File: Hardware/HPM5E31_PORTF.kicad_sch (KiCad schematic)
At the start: 1 part, among them U1 HPM5E31IGN1

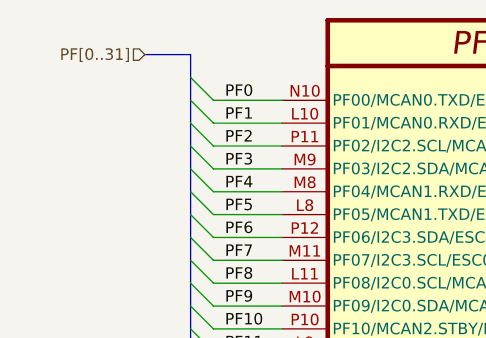
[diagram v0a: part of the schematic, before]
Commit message: 新增ESC IO引出，ESC CTR LED，EUI接口
编码器接口电源输出加保险，SPI加ESD
PY32ADC外部接口加ESD
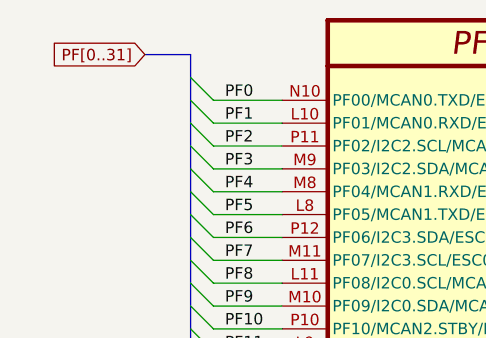
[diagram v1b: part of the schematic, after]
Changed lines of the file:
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@@
 		)
 	)
-	(hierarchical_label "PF[0..31]"
+	(global_label "PF[0..31]"
 		(shape input)
 		(at 90.17 53.34 180)
+		(fields_autoplaced yes)
 		(effects
 			(font
@@
 			(justify right)
 		)
+		(property "Intersheetrefs" "${INTERSHEET_REFS}"
+			(at 78.2947 53.34 0)
+			(effects
+				(font
+					(size 1.27 1.27)
+				)
+				(justify right)
+				(hide yes)
+			)
+		)
 	)

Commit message: 拉线
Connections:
- net PF0: now also U1.M2 (DCDC_IN); no longer U1.N10 (PF00/MCAN0.TXD/ESC0.MDC/PWM0.P0/TRGM.P00/ETH0.MDC/QEO1.A)
- net PF1: no longer U1.L10 (PF01/MCAN0.RXD/ESC0.MDIO/PWM0.P1/TRGM.P01/ETH0.MDIO/QEO1.B)
- net PF10: no longer U1.P10 (PF10/MCAN2.STBY/ESC0.P1_RXD1/PWM1.P2/TRGM.P10/ETH0.RXD1/EUI1.DI)
- net PF11: no longer U1.L9 (PF11/ESC0.P1_RXD2/PWM1.P3/TRGM.P11/ETH0.RXD2/EUI1.DO)
- net PF12: no longer U1.N11 (PF12/I2C1.SDA/ESC0.P1_RXD3/PWM1.P4/TRGM.P12/ETH0.RXD3/OWR0.DAT)
- net PF13: no longer U1.N12 (PF13/I2C1.SCL/MCAN3.STBY/ESC0.P1_RXCK/PWM1.P5/TRGM.P13/ETH0.RXCK/OWR1.DAT)
- net PF14: no longer U1.N9 (PF14/MCAN3.RXD/ESC0.P1_RXER/PWM1.P6/TRGM.P14/ETH0.RXER)
- net PF15: no longer U1.P9 (PF15/MCAN3.TXD/PWM1.P7/TRGM.P15/ETH0.TXER)
- net PF16: no longer U1.N7 (PF16/SDM0.DAT0/ADC0.IN08/ADC1.IN08/ACMP0_CH0.INN7)
- net PF17: no longer U1.P7 (PF17/SDM0.CLK0/ADC0.IN12/ADC1.IN12/ACMP0_CH1.INN7)
- net PF18: no longer U1.P8 (PF18/SDM0.DAT1/USB0.PWR/ETH0.EVTO0/ESC0.EVTO0/ADC0.IN11/ADC1.IN11/ACMP0_CH1.INP7)
- net PF19: no longer U1.M5 (PF19/SDM0.CLK1/USB0.PWR/ADC0.IN13/ADC1.IN13/ACMP0_CH0.INP7)
- net PF2: no longer U1.P11 (PF02/I2C2.SCL/MCAN0.STBY/ESC0.P1_TXCK/PWM0.P2/TRGM.P02/ETH0.TXCK/QEI0.H1/QEO1.Z/EUI0.CK)
- net PF20: no longer U1.N6 (PF20/SDM0.DAT3/USB0.OC/ETH0.EVTO1/ESC0.EVTO1/ADC0.IN03/ADC1.IN03/ACMP0_CH0.INP4/ACMP0_CH1.INP4)
- net PF21: no longer U1.L6 (PF21/SDM0.DAT2/USB0.ID/ETH0.EVTI0/ESC0.EVTI0/ADC0.IN02/ADC1.IN02/ACMP0_CH0.INN4/ACMP0_CH1.INN4)
- net PF22: no longer U1.N8 (PF22/SDM0.CLK2/USB0.ID/ETH0.EVTI1/ESC0.EVTI1/ADC0.IN14/ADC1.IN14/ACMP0_CH0.INN5/ACMP0_CH1.INN5)
- net PF23: no longer U1.L5 (PF23/SDM0.CLK3/USB0.OC/ADC0.IN15/ADC1.IN15/ACMP0_CH0.INN3/ACMP0_CH1.INN3)
- net PF24: no longer U1.M6 (PF24/SDM0.DAT0/ADC0.IN10/ADC1.IN10/ACMP0_CH0.INP5/ACMP0_CH1.INP5)
- net PF25: no longer U1.L7 (PF25/SDM0.CLK0/ADC0.IN09/ADC1.IN09/ACMP0_CH0.INP3/ACMP0_CH1.INP3)
- net PF26: no longer U1.P6 (PF26/SDM0.DAT1/ADC0.IN01/ADC1.IN01/ACMP0_CH0.INN6/ACMP0_CH1.INN6)
- net PF27: no longer U1.M7 (PF27/SDM0.CLK1/ADC0.IN00/ADC1.IN00/ACMP0_CH0.INP6/ACMP0_CH1.INP6)
- net PF28: no longer U1.P5 (PF28/SDM0.DAT3/ADC0.IN05/ADC1.IN05/ACMP0_CH0.INN2/ACMP0_CH1.INN2)
- net PF29: no longer U1.M4 (PF29/SDM0.DAT2/ADC0.IN04/ADC1.IN04/ACMP0_CH0.INP2/ACMP0_CH1.INP2)
- net PF3: now also U1.N2 (DCDC_LP); no longer U1.M9 (PF03/I2C2.SDA/MCAN1.STBY/ESC0.P1_TXD0/PWM0.P3/TRGM.P03/ETH0.TXD0/QEI0.F/EUI0.SH)
- net PF30: no longer U1.L4 (PF30/SDM0.CLK2/ADC0.IN06/ADC1.IN06/ACMP0_CH0.INN1/ACMP0_CH1.INN1)
- net PF31: no longer U1.N5 (PF31/SDM0.CLK3/ADC0.IN07/ADC1.IN07/ACMP0_CH0.INP1/ACMP0_CH1.INP1)
- net PF4: now also U1.P3 (DCDC_LP); no longer U1.M8 (PF04/MCAN1.RXD/ESC0.P1_TXD1/PWM0.P4/TRGM.P04/ETH0.TXD1/QEI0.H0/EUI0.DI)
- net PF5: no longer U1.L8 (PF05/MCAN1.TXD/ESC0.P1_TXD2/PWM0.P5/TRGM.P05/ETH0.TXD2/QEI0.Z/QEO0.Z/EUI0.DO)
- net PF6: no longer U1.P12 (PF06/I2C3.SDA/ESC0.P1_TXD3/PWM0.P6/TRGM.P06/ETH0.TXD3/QEI0.B/QEO0.B)
- net PF7: no longer U1.M11 (PF07/I2C3.SCL/ESC0.P1_TXEN/PWM0.P7/TRGM.P07/ETH0.TXEN/QEI0.A/QEO0.A)
- net PF8: no longer U1.L11 (PF08/I2C0.SCL/MCAN2.TXD/ESC0.P1_RXDV/PWM1.P0/TRGM.P08/ETH0.RXDV/EUI1.CK)
- net PF9: no longer U1.M10 (PF09/I2C0.SDA/MCAN2.RXD/ESC0.P1_RXD0/PWM1.P1/TRGM.P09/ETH0.RXD0/EUI1.SH)
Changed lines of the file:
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@@
 		(lib_id "HPM5E00_Library:HPM5E31IGN1")
 		(at 110.49 49.53 0)
-		(unit 9)
+		(unit 1)
 		(exclude_from_sim no)
 		(in_bom yes)
@@
 		(pin "L6"
 		)
-		(instances
-			(project "HPM5E31_ECatDualFOC"
-				(path "/a07e9810-3899-4327-ba8f-f24142a7c70e/b9a8d5a3-7d25-4818-87f6-adc719379948/8f0ee0c1-87cd-4b65-b034-417b791c254b"
-					(reference "U1")
-					(unit 9)
-				)
-			)
-		)
 	)

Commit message: 修存档拉线
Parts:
- renumbered U1 to U3
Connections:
- net PF0: now also U3.N10 (PF00/MCAN0.TXD/ESC0.MDC/PWM0.P0/TRGM.P00/ETH0.MDC/QEO1.A); no longer U3.M2 (DCDC_IN)
- net PF1: now also U3.L10 (PF01/MCAN0.RXD/ESC0.MDIO/PWM0.P1/TRGM.P01/ETH0.MDIO/QEO1.B)
- net PF10: now also U3.P10 (PF10/MCAN2.STBY/ESC0.P1_RXD1/PWM1.P2/TRGM.P10/ETH0.RXD1/EUI1.DI)
- net PF11: now also U3.L9 (PF11/ESC0.P1_RXD2/PWM1.P3/TRGM.P11/ETH0.RXD2/EUI1.DO)
- net PF12: now also U3.N11 (PF12/I2C1.SDA/ESC0.P1_RXD3/PWM1.P4/TRGM.P12/ETH0.RXD3/OWR0.DAT)
- net PF13: now also U3.N12 (PF13/I2C1.SCL/MCAN3.STBY/ESC0.P1_RXCK/PWM1.P5/TRGM.P13/ETH0.RXCK/OWR1.DAT)
- net PF14: now also U3.N9 (PF14/MCAN3.RXD/ESC0.P1_RXER/PWM1.P6/TRGM.P14/ETH0.RXER)
- net PF15: now also U3.P9 (PF15/MCAN3.TXD/PWM1.P7/TRGM.P15/ETH0.TXER)
- net PF16: now also U3.N7 (PF16/SDM0.DAT0/ADC0.IN08/ADC1.IN08/ACMP0_CH0.INN7)
- net PF17: now also U3.P7 (PF17/SDM0.CLK0/ADC0.IN12/ADC1.IN12/ACMP0_CH1.INN7)
- net PF18: now also U3.P8 (PF18/SDM0.DAT1/USB0.PWR/ETH0.EVTO0/ESC0.EVTO0/ADC0.IN11/ADC1.IN11/ACMP0_CH1.INP7)
- net PF19: now also U3.M5 (PF19/SDM0.CLK1/USB0.PWR/ADC0.IN13/ADC1.IN13/ACMP0_CH0.INP7)
- net PF2: now also U3.P11 (PF02/I2C2.SCL/MCAN0.STBY/ESC0.P1_TXCK/PWM0.P2/TRGM.P02/ETH0.TXCK/QEI0.H1/QEO1.Z/EUI0.CK)
- net PF20: now also U3.N6 (PF20/SDM0.DAT3/USB0.OC/ETH0.EVTO1/ESC0.EVTO1/ADC0.IN03/ADC1.IN03/ACMP0_CH0.INP4/ACMP0_CH1.INP4)
- net PF21: now also U3.L6 (PF21/SDM0.DAT2/USB0.ID/ETH0.EVTI0/ESC0.EVTI0/ADC0.IN02/ADC1.IN02/ACMP0_CH0.INN4/ACMP0_CH1.INN4)
- net PF22: now also U3.N8 (PF22/SDM0.CLK2/USB0.ID/ETH0.EVTI1/ESC0.EVTI1/ADC0.IN14/ADC1.IN14/ACMP0_CH0.INN5/ACMP0_CH1.INN5)
- net PF23: now also U3.L5 (PF23/SDM0.CLK3/USB0.OC/ADC0.IN15/ADC1.IN15/ACMP0_CH0.INN3/ACMP0_CH1.INN3)
- net PF24: now also U3.M6 (PF24/SDM0.DAT0/ADC0.IN10/ADC1.IN10/ACMP0_CH0.INP5/ACMP0_CH1.INP5)
- net PF25: now also U3.L7 (PF25/SDM0.CLK0/ADC0.IN09/ADC1.IN09/ACMP0_CH0.INP3/ACMP0_CH1.INP3)
- net PF26: now also U3.P6 (PF26/SDM0.DAT1/ADC0.IN01/ADC1.IN01/ACMP0_CH0.INN6/ACMP0_CH1.INN6)
- net PF27: now also U3.M7 (PF27/SDM0.CLK1/ADC0.IN00/ADC1.IN00/ACMP0_CH0.INP6/ACMP0_CH1.INP6)
- net PF28: now also U3.P5 (PF28/SDM0.DAT3/ADC0.IN05/ADC1.IN05/ACMP0_CH0.INN2/ACMP0_CH1.INN2)
- net PF29: now also U3.M4 (PF29/SDM0.DAT2/ADC0.IN04/ADC1.IN04/ACMP0_CH0.INP2/ACMP0_CH1.INP2)
- net PF3: now also U3.M9 (PF03/I2C2.SDA/MCAN1.STBY/ESC0.P1_TXD0/PWM0.P3/TRGM.P03/ETH0.TXD0/QEI0.F/EUI0.SH); no longer U3.N2 (DCDC_LP)
- net PF30: now also U3.L4 (PF30/SDM0.CLK2/ADC0.IN06/ADC1.IN06/ACMP0_CH0.INN1/ACMP0_CH1.INN1)
- net PF31: now also U3.N5 (PF31/SDM0.CLK3/ADC0.IN07/ADC1.IN07/ACMP0_CH0.INP1/ACMP0_CH1.INP1)
- net PF4: now also U3.M8 (PF04/MCAN1.RXD/ESC0.P1_TXD1/PWM0.P4/TRGM.P04/ETH0.TXD1/QEI0.H0/EUI0.DI); no longer U3.P3 (DCDC_LP)
- net PF5: now also U3.L8 (PF05/MCAN1.TXD/ESC0.P1_TXD2/PWM0.P5/TRGM.P05/ETH0.TXD2/QEI0.Z/QEO0.Z/EUI0.DO)
- net PF6: now also U3.P12 (PF06/I2C3.SDA/ESC0.P1_TXD3/PWM0.P6/TRGM.P06/ETH0.TXD3/QEI0.B/QEO0.B)
- net PF7: now also U3.M11 (PF07/I2C3.SCL/ESC0.P1_TXEN/PWM0.P7/TRGM.P07/ETH0.TXEN/QEI0.A/QEO0.A)
- net PF8: now also U3.L11 (PF08/I2C0.SCL/MCAN2.TXD/ESC0.P1_RXDV/PWM1.P0/TRGM.P08/ETH0.RXDV/EUI1.CK)
- net PF9: now also U3.M10 (PF09/I2C0.SDA/MCAN2.RXD/ESC0.P1_RXD0/PWM1.P1/TRGM.P09/ETH0.RXD0/EUI1.SH)
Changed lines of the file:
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@@
 		(lib_id "HPM5E00_Library:HPM5E31IGN1")
 		(at 110.49 49.53 0)
-		(unit 1)
+		(unit 9)
 		(exclude_from_sim no)
 		(in_bom yes)
@@
 		(dnp no)
 		(fields_autoplaced yes)
-		(property "Reference" "U1"
+		(property "Reference" "U3"
 			(at 223.52 93.9799 0)
 			(effects
@@
 		(pin "L6"
 		)
+		(instances
+			(project "HPM5E31_ECatDualFOC"
+				(path "/a07e9810-3899-4327-ba8f-f24142a7c70e/b9a8d5a3-7d25-4818-87f6-adc719379948/8f0ee0c1-87cd-4b65-b034-417b791c254b"
+					(reference "U3")
+					(unit 9)
+				)
+			)
+		)
 	)
